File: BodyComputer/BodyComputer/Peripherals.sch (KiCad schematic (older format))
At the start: 28 parts, among them J10 Conn_02x03_Odd_Even, J11 SS-6488-FLS, J12 USB_B_Mini, J13 Conn_02x05_Odd_Even, J14 Conn_02x05_Odd_Even, J35 Conn_01x02, J37 Conn_01x02, J39 Conn_01x02, J9 Conn_02x05_Odd_Even, Q1 Q_NPN_BCE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

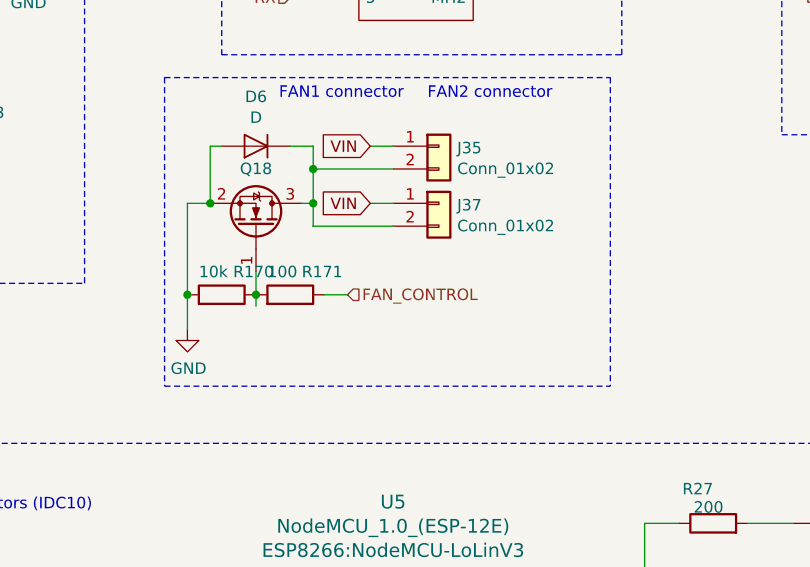
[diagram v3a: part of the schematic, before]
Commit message: Body Computer [DONE]
Body Computer done as a 2-layer board and put into prototype production, schematics and PCBs created.
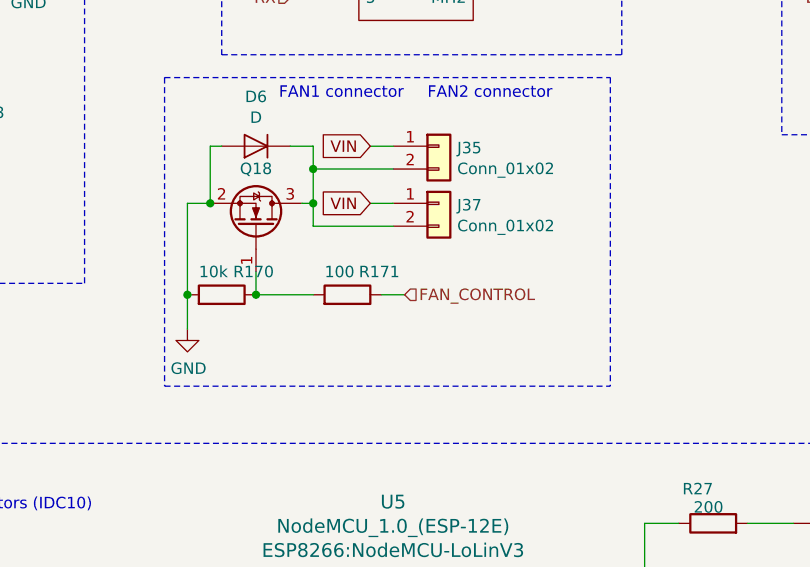
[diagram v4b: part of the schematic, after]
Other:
- moved on the sheet: R171
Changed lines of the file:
@@
 Sheet 4 7
 Title "Body Computer"
-Date "2020-04-12"
+Date "2020-04-17"
 Rev "1.0"
 Comp "Wojciech Grzeliński"
@@
 L Device:R R?
 U 1 1 5E9991C0
-P 3700 2950
+P 3950 2950
 AR Path="/5E667041/5E9991C0" Ref="R?"  Part="1"
 AR Path="/5E731526/5E9991C0" Ref="R?"  Part="1"
 AR Path="/5E6DC799/5E9991C0" Ref="R171"  Part="1"
-F 0 "R171" V 3800 3000 50  0000 L CNN
-F 1 "100" V 3800 2850 50  0000 L CNN
-F 2 "Resistor_SMD:R_0603_1608Metric" V 3630 2950 50  0001 C CNN
-F 3 "~" H 3700 2950 50  0001 C CNN
-	1    3700 2950
+F 0 "R171" V 4050 3000 50  0000 L CNN
+F 1 "100" V 4050 2850 50  0000 L CNN
+F 2 "Resistor_SMD:R_0603_1608Metric" V 3880 2950 50  0001 C CNN
+F 3 "~" H 3950 2950 50  0001 C CNN
+	1    3950 2950
 	0    1    -1   0
 $EndComp
@@
 $EndComp
 Wire Wire Line
-	3550 3000 3550 2950
-Wire Wire Line
 	3550 2850 3550 2950
 Connection ~ 3550 2950
@@
 Connection ~ 3250 2950
 Wire Wire Line
-	3850 2950 3950 2950
+	4100 2950 4200 2950
 Wire Wire Line
 	3800 2650 3800 2550
@@
 Wire Notes Line
 	3150 3350 5100 3350
-Text HLabel 3950 2950 2    50   Input ~ 0
+Text HLabel 4200 2950 2    50   Input ~ 0
 FAN_CONTROL
 $Comp
@@
 Wire Wire Line
 	3050 5750 3350 5750
+Wire Wire Line
+	3800 2950 3550 2950
 $EndSCHEMATC
